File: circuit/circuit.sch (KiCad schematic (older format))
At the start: 59 parts, among them J1 Conn_01x20_Female, J2 Conn_02x03_Odd_Even, P1 CONN_02X03, U1 LMC6484, U10 ATmega328P-PU, U2 LIS3DHTR, U3 LM358DT, U4 LM358DT, U5 L78M05CDT-TR, U6 LM3480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

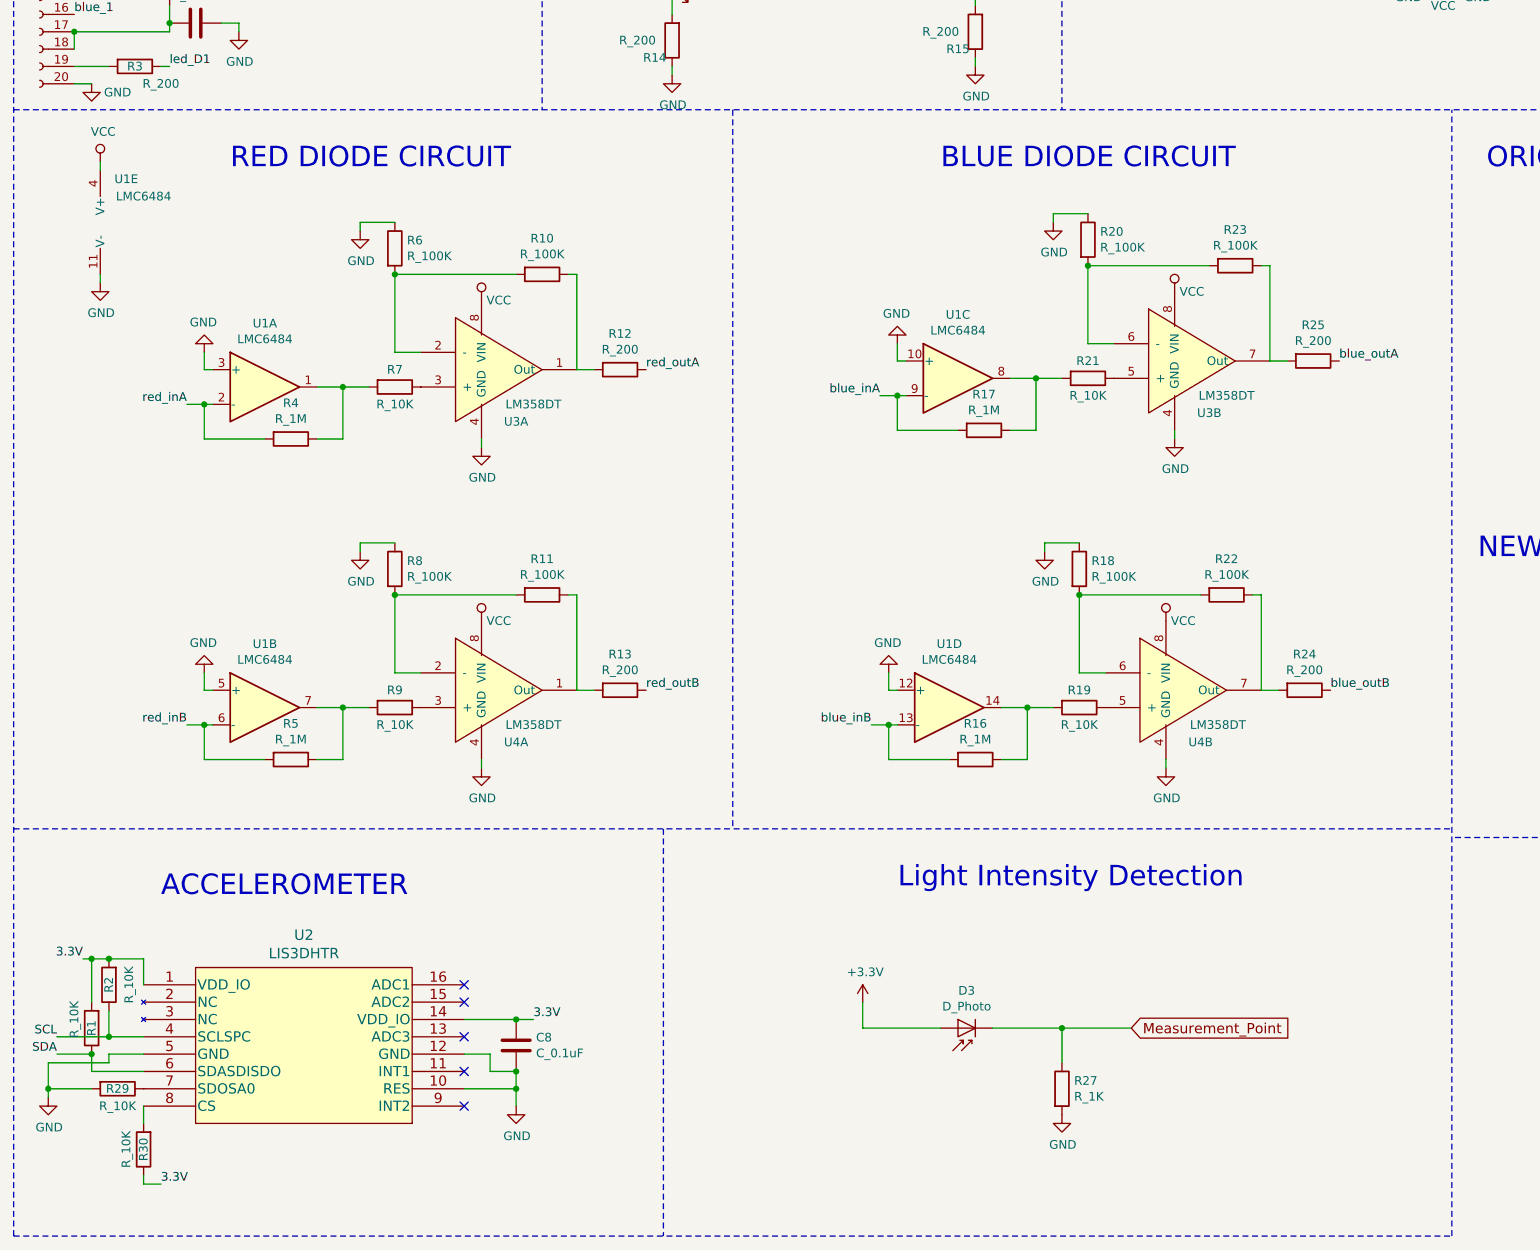
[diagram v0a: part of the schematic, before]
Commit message: Added a new LED  circuit
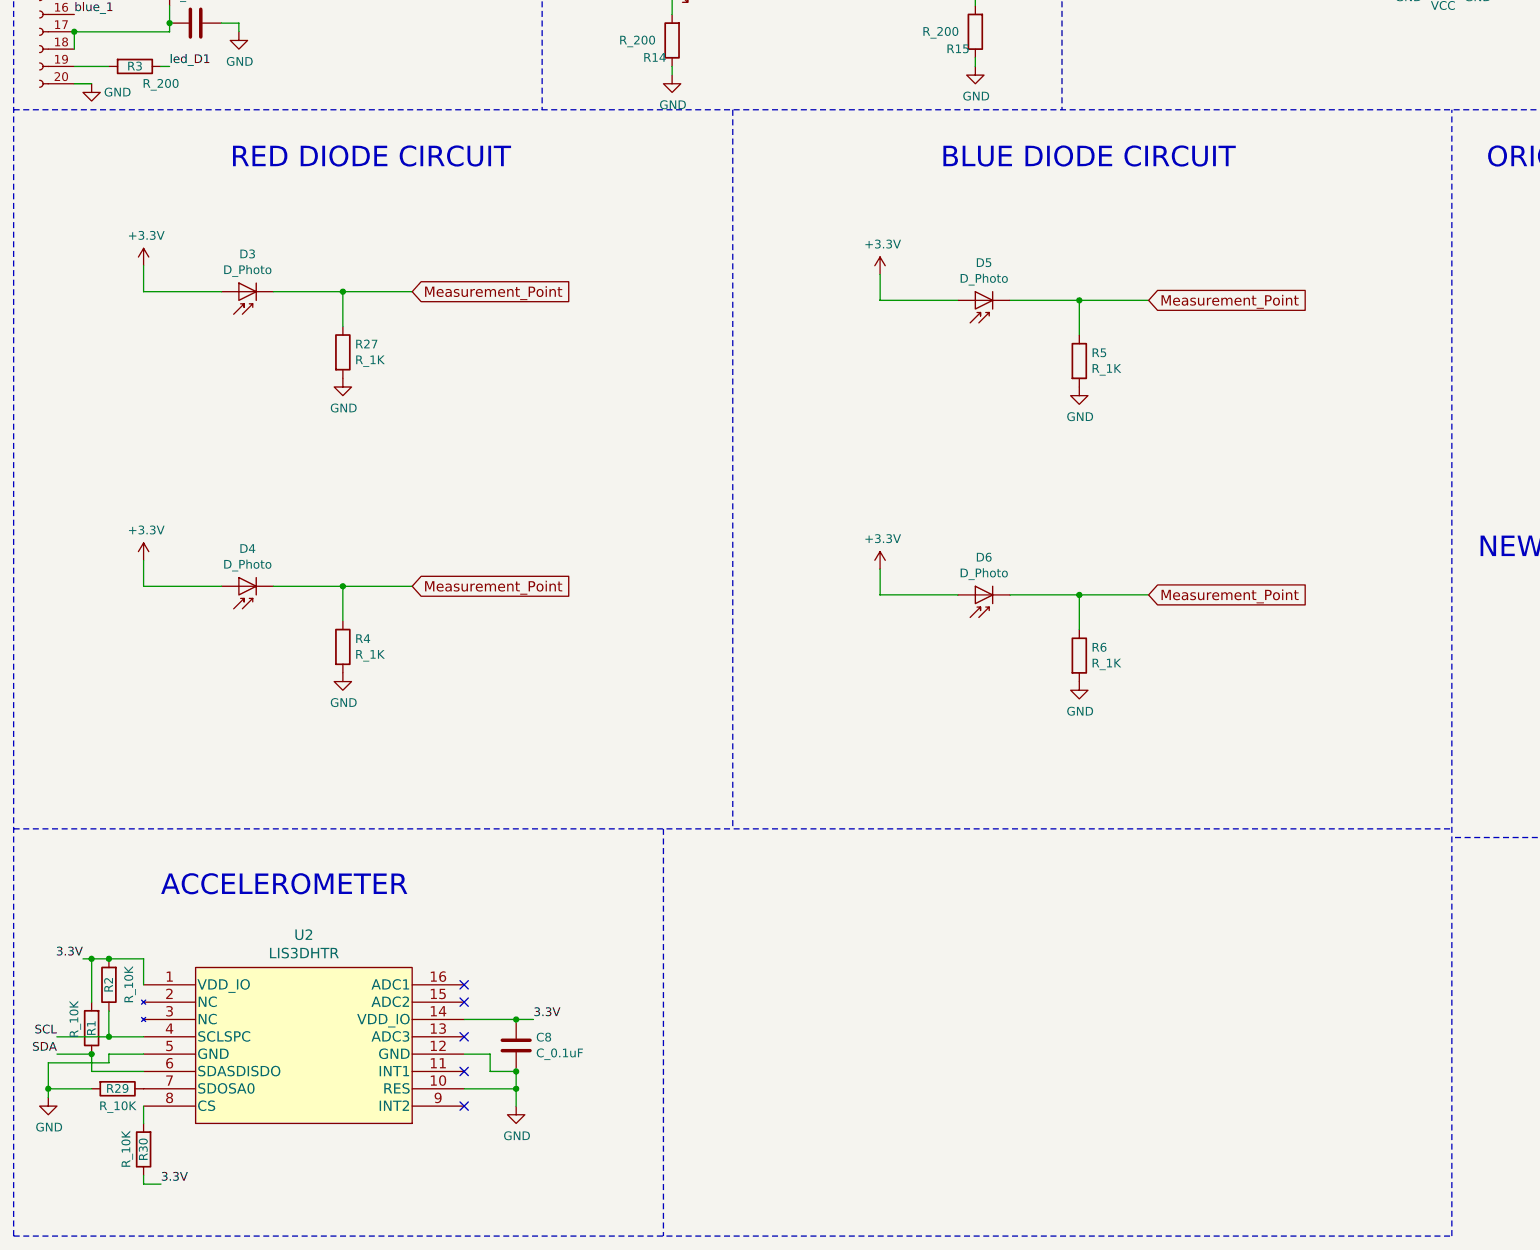
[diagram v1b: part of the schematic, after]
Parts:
- removed R10, R11, R18, R20, R22, R23, R6, R8: R_100K, footprints:R_0805_OEM, symbol formula:R_100K
- removed R12, R13, R24, R25: R_200, footprints:R_0805_OEM, symbol formula:R_200
- removed R16, R17, R4, R5: R_1M, footprints:R_0805_OEM, symbol formula:R_1M
- removed R19, R21, R7, R9: R_10K, footprints:R_0805_OEM, symbol formula:R_10K
- removed U1: LMC6484, Housings_SOIC:SOIC-14_3.9x8.7mm_Pitch1.27mm, symbol Amplifier_Operational:LMC6484
- removed U3, U4: LM358DT, Housings_SOIC:SO-8_5.3x6.2mm_Pitch1.27mm, symbol formula:LM358DT
- added D4, D5, D6: D_Photo, symbol Device:D_Photo
- added R4, R5, R6: R_1K, footprints:R_0805_OEM, symbol formula:R_1K
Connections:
- wire segments 217 -> 154
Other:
- note removed: "Light Intensity Detection"
- moved on the sheet: D3, R27
